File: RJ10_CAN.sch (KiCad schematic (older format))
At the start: 1 part

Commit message: Perform layout. Add CAN testpoints.
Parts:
- gave numbers to parts that had none: 1
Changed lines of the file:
@@
 $Descr A4 11693 8268
 encoding utf-8
-Sheet 4 12
+Sheet 12 16
 Title "CAN Distributor"
 Date "2021-04-03"
@@
 	5900 3900 6250 3900
 $Comp
-L Connector:RJ10 J?
+L Connector:RJ10 J4
 U 1 1 6068392D
 P 5500 3900
-AR Path="/60682F6E/6068392D" Ref="J?"  Part="1"
-AR Path="/6069ABE0/6068392D" Ref="J?"  Part="1"
-AR Path="/6069AD3C/6068392D" Ref="J?"  Part="1"
-AR Path="/6069AD3E/6068392D" Ref="J?"  Part="1"
-AR Path="/6069AE53/6068392D" Ref="J?"  Part="1"
-AR Path="/6069B12F/6068392D" Ref="J?"  Part="1"
-AR Path="/6069B131/6068392D" Ref="J?"  Part="1"
-AR Path="/6069B133/6068392D" Ref="J?"  Part="1"
-AR Path="/6069B135/6068392D" Ref="J?"  Part="1"
-F 0 "J?" H 5557 4367 50  0000 C CNN
+AR Path="/60682F6E/6068392D" Ref="J4"  Part="1"
+AR Path="/6069ABE0/6068392D" Ref="J5"  Part="1"
+AR Path="/6069AD3C/6068392D" Ref="J6"  Part="1"
+AR Path="/6069AD3E/6068392D" Ref="J7"  Part="1"
+AR Path="/6069AE53/6068392D" Ref="J8"  Part="1"
+AR Path="/6069B12F/6068392D" Ref="J9"  Part="1"
+AR Path="/6069B131/6068392D" Ref="J10"  Part="1"
+AR Path="/6069B133/6068392D" Ref="J11"  Part="1"
+AR Path="/6069B135/6068392D" Ref="J12"  Part="1"
+F 0 "J12" H 5557 4367 50  0000 C CNN
 F 1 "RJ10" H 5557 4276 50  0000 C CNN
 F 2 "CAN-Distributor:TE_5520257-2" V 5500 3950 50  0001 C CNN

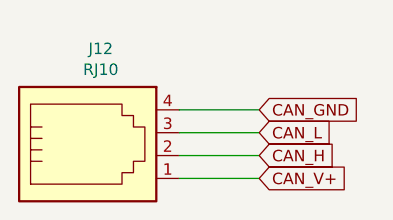
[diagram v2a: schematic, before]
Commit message: Add protection TVS and GDT. Rename TP file.
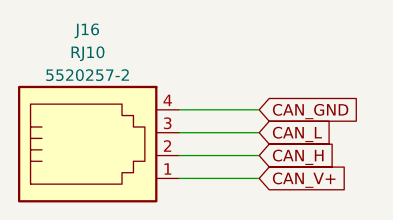
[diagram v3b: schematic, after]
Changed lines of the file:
@@
 $Descr A4 11693 8268
 encoding utf-8
-Sheet 12 16
+Sheet 15 16
 Title "CAN Distributor"
-Date "2021-04-03"
-Rev "2.0"
+Date "2021-04-04"
+Rev "2.1"
 Comp ""
 Comment1 "Designed by: Erik Almbratt"
@@
 AR Path="/6069B133/6068392D" Ref="J11"  Part="1"
 AR Path="/6069B135/6068392D" Ref="J12"  Part="1"
-AR Path="/606AA4F3/6068392D" Ref="J?"  Part="1"
-F 0 "J12" H 5557 4367 50  0000 C CNN
-F 1 "RJ10" H 5557 4276 50  0000 C CNN
+AR Path="/606AA4F3/6068392D" Ref="J16"  Part="1"
+F 0 "J16" H 5500 4450 50  0000 C CNN
+F 1 "RJ10" H 5500 4350 50  0000 C CNN
 F 2 "CAN-Distributor:TE_5520257-2" V 5500 3950 50  0001 C CNN
 F 3 "https://www.te.com/commerce/DocumentDelivery/DDEController?Action=showdoc&DocId=Customer+Drawing%7F5520257%7FB1%7Fpdf%7FEnglish%7FENG_CD_5520257_B1.pdf%7F5520257-2" V 5500 3950 50  0001 C CNN
 F 4 "1284339" H 5500 3900 50  0001 C CNN "Farnell"
-F 5 "5520257-2" H 5500 3900 50  0001 C CNN "MPN"
+F 5 "5520257-2" H 5500 4250 50  0000 C CNN "MPN"
 F 6 "TE Connectivity" H 5500 3900 50  0001 C CNN "Manufacturer"
 	1    5500 3900
